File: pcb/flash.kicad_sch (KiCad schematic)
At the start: 5 parts, among them U8 GD5F2GM7UEYIGR

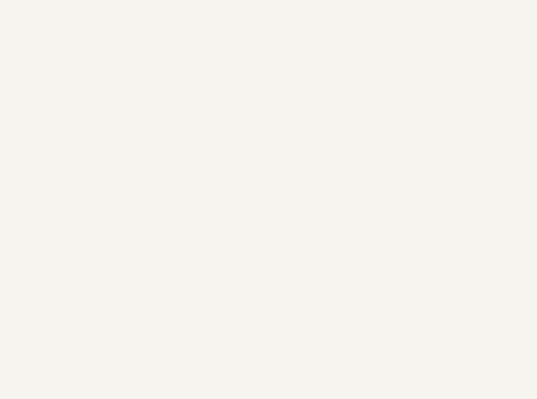
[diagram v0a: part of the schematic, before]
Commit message: sch: adjust test points
Removes some test points, and adds useful ones to data lines. Fixes #19
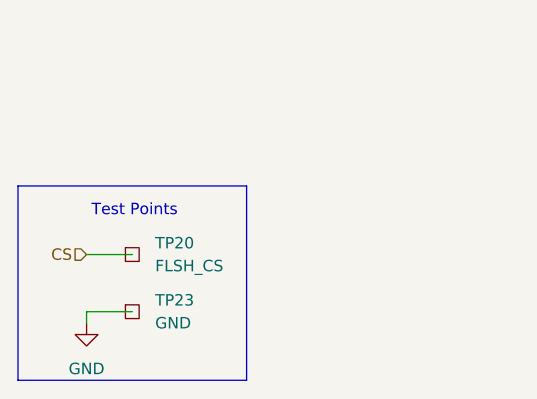
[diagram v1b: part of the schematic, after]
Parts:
- added TP20: FLSH_CS, TestPoint:TestPoint_Pad_D1.0mm, symbol Connector:TestPoint_Square
- added TP23: GND, TestPoint:TestPoint_Plated_Hole_D2.0mm, symbol Connector:TestPoint_Square
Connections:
- net CS: now also TP20.1
- net GND: now also TP23.1
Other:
- note added: "Test Points"

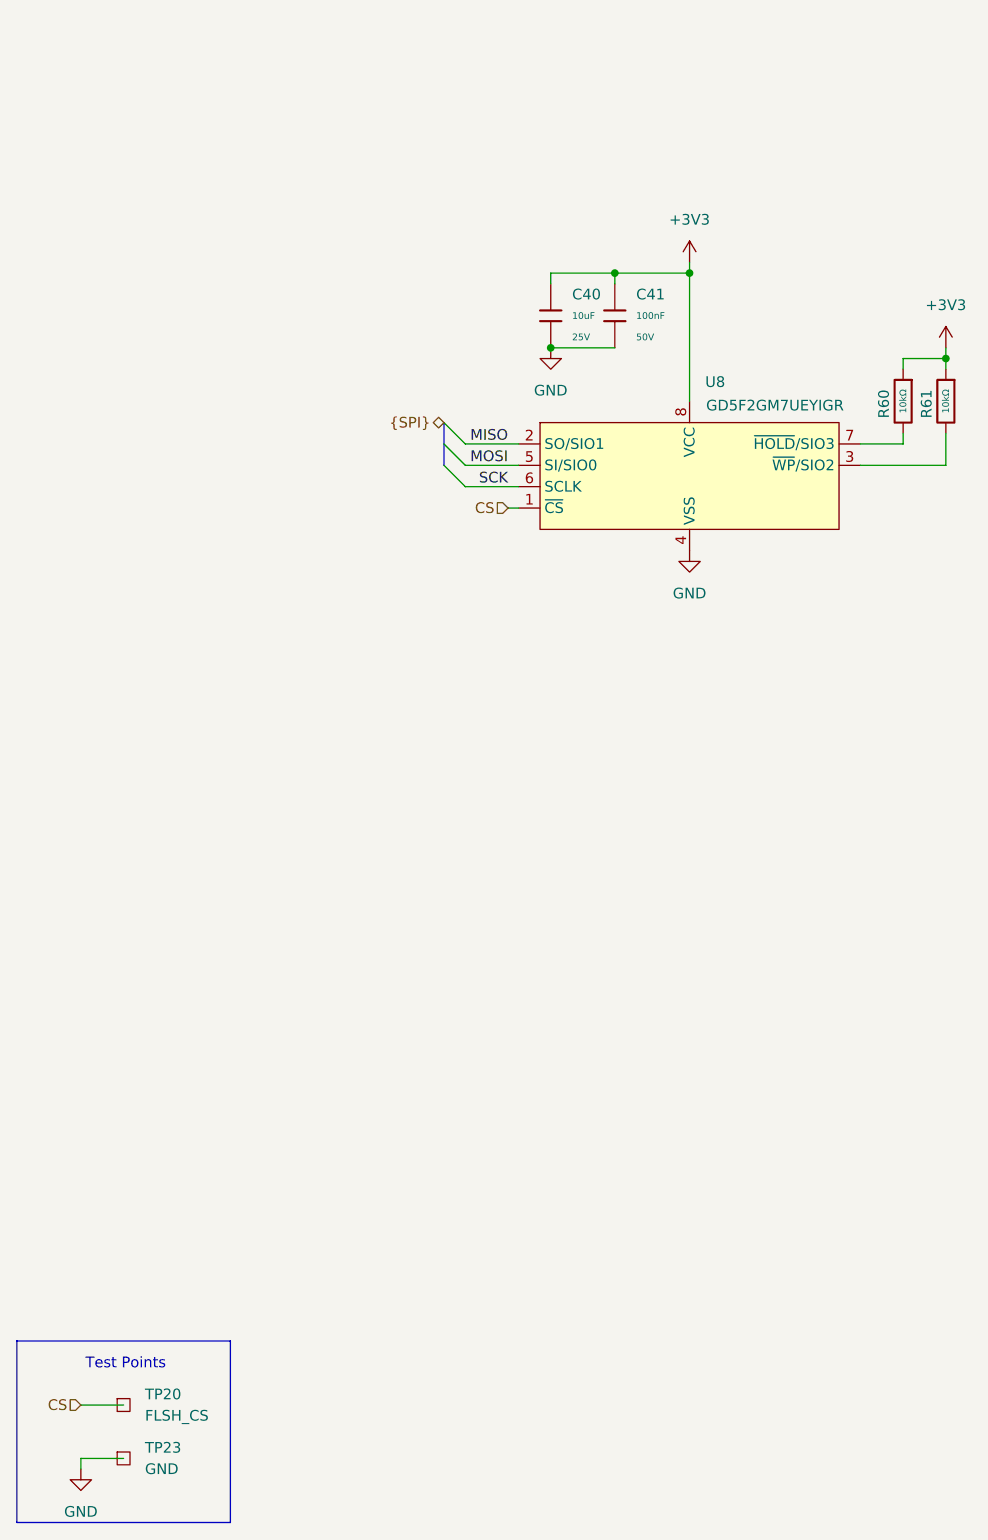
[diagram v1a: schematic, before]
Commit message: sch: add schematic titles and do some cleanup
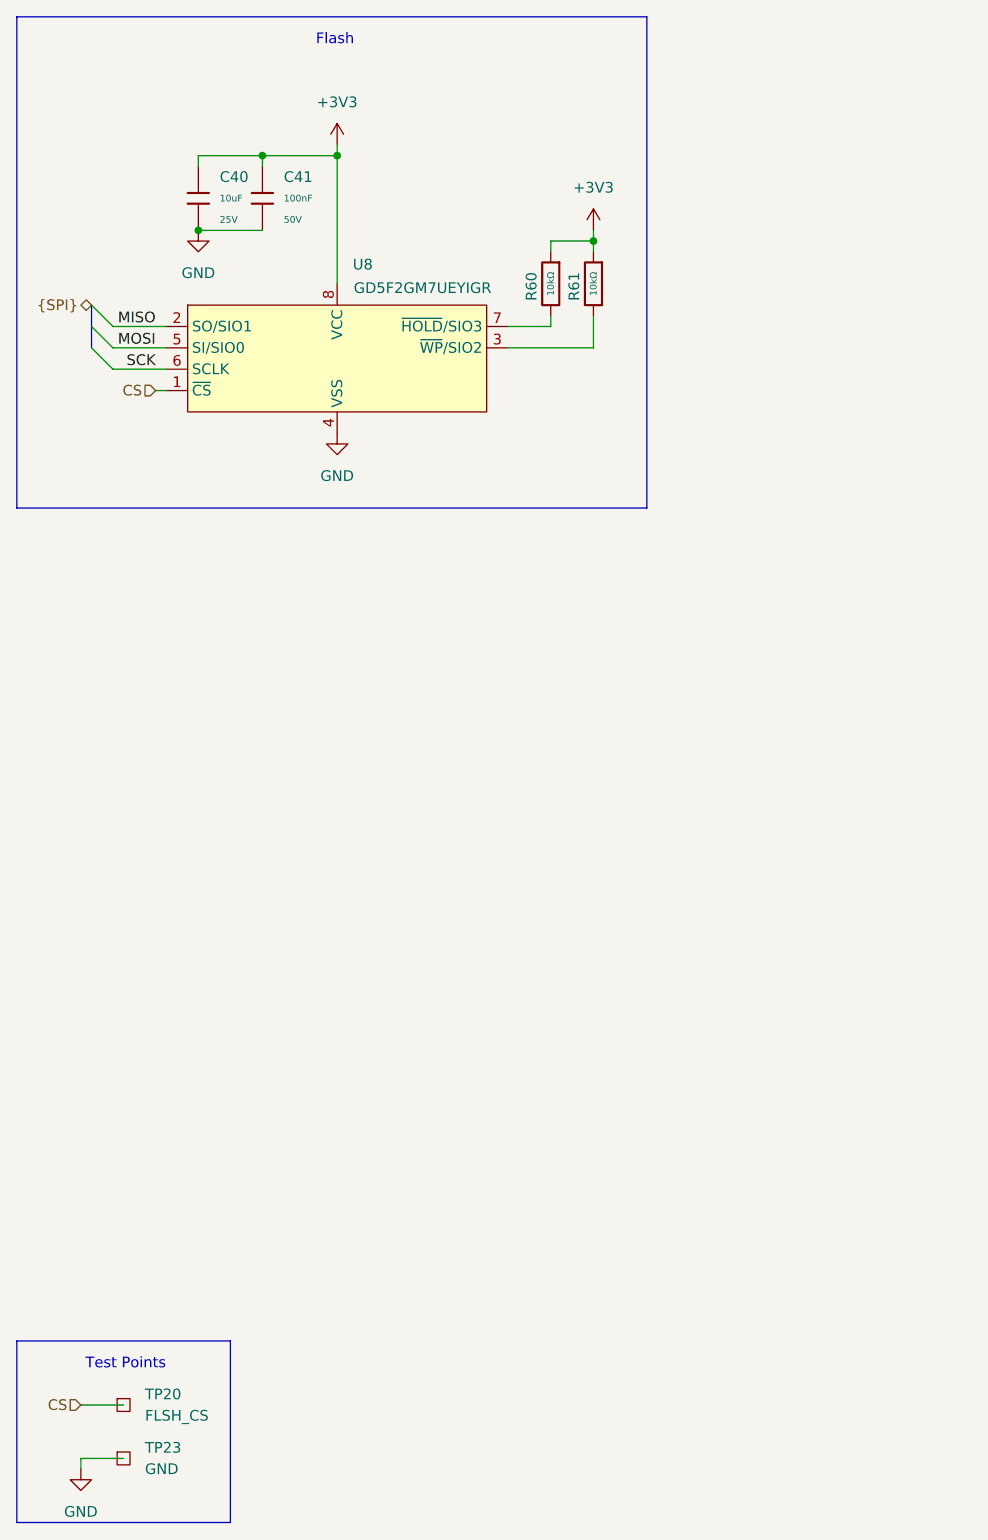
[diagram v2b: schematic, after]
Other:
- note added: "Flash"
- company: (none) -> CIA Assured
- title: (none) -> Flash Storage
- moved on the sheet: C40, C41, R60, R61, U8
